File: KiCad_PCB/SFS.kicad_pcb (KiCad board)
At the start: 2 copper layers, 76.2 x 106.7 mm, 40 parts, among them J1 Screw_Terminal_01x08, J2 Conn_01x06, J4 Screw_Terminal_01x02, J6 Screw_Terminal_01x04, Q1 IRF9540N, Q2 IRLB4132, Q3 2N7000, SW1 SW_Push, SW2 SW_Push, U2 ADS1115, U3 ADS1115, U4 DS3231, U6 L7806, U7 LT1460

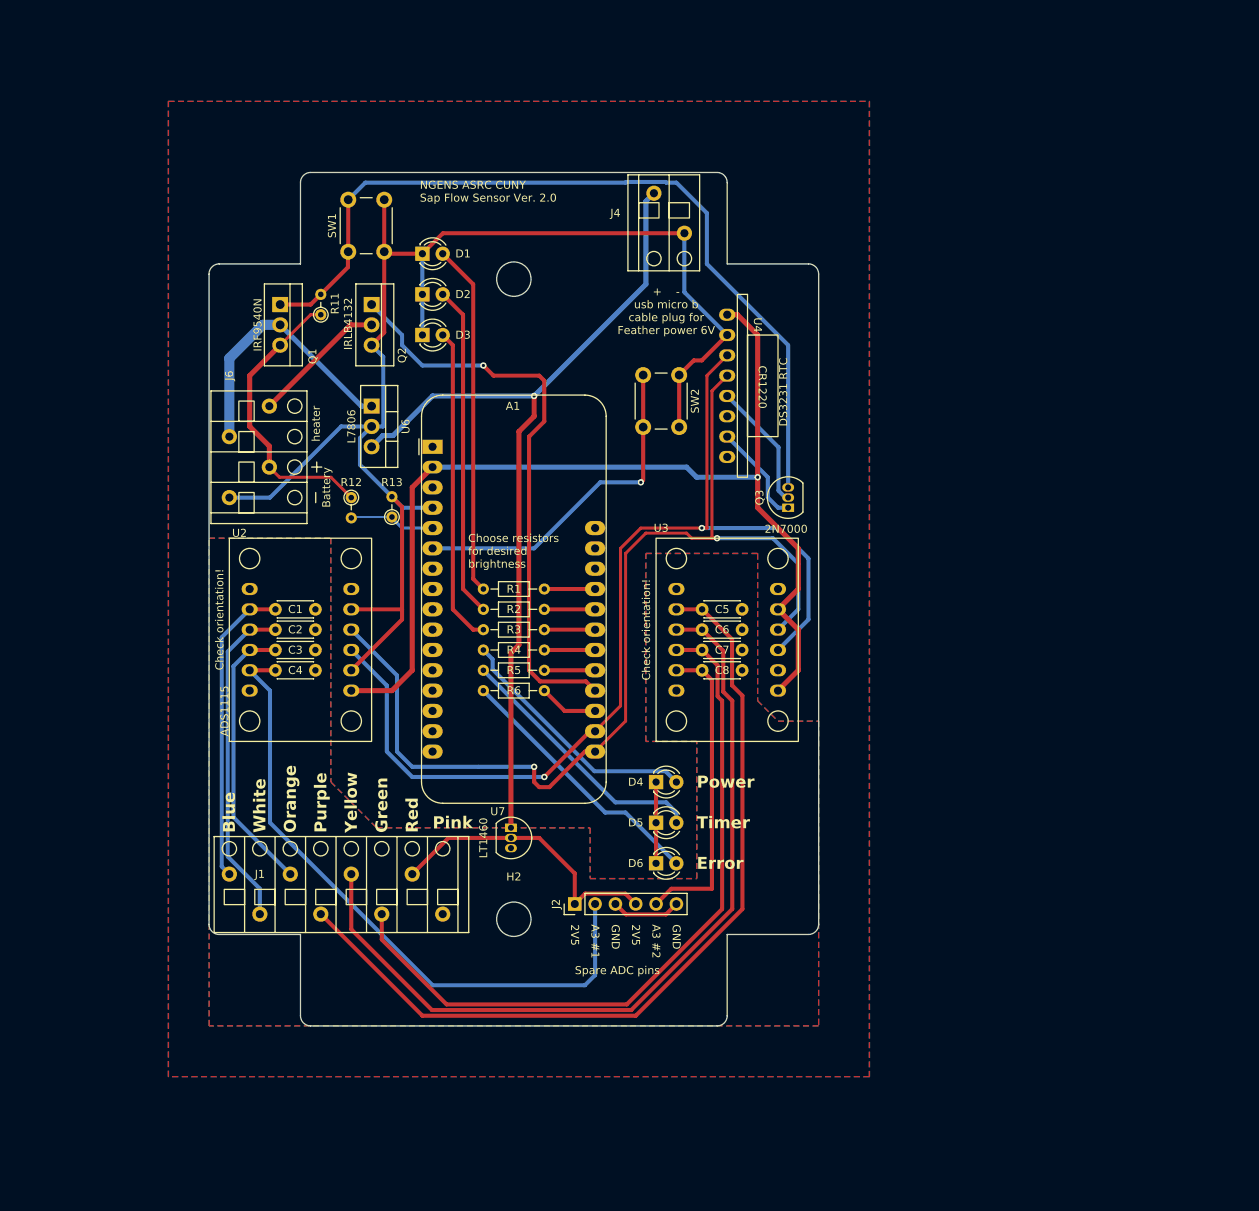
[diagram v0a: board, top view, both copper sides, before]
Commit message: updated kicad
Updated to v2.1 from evonne's github
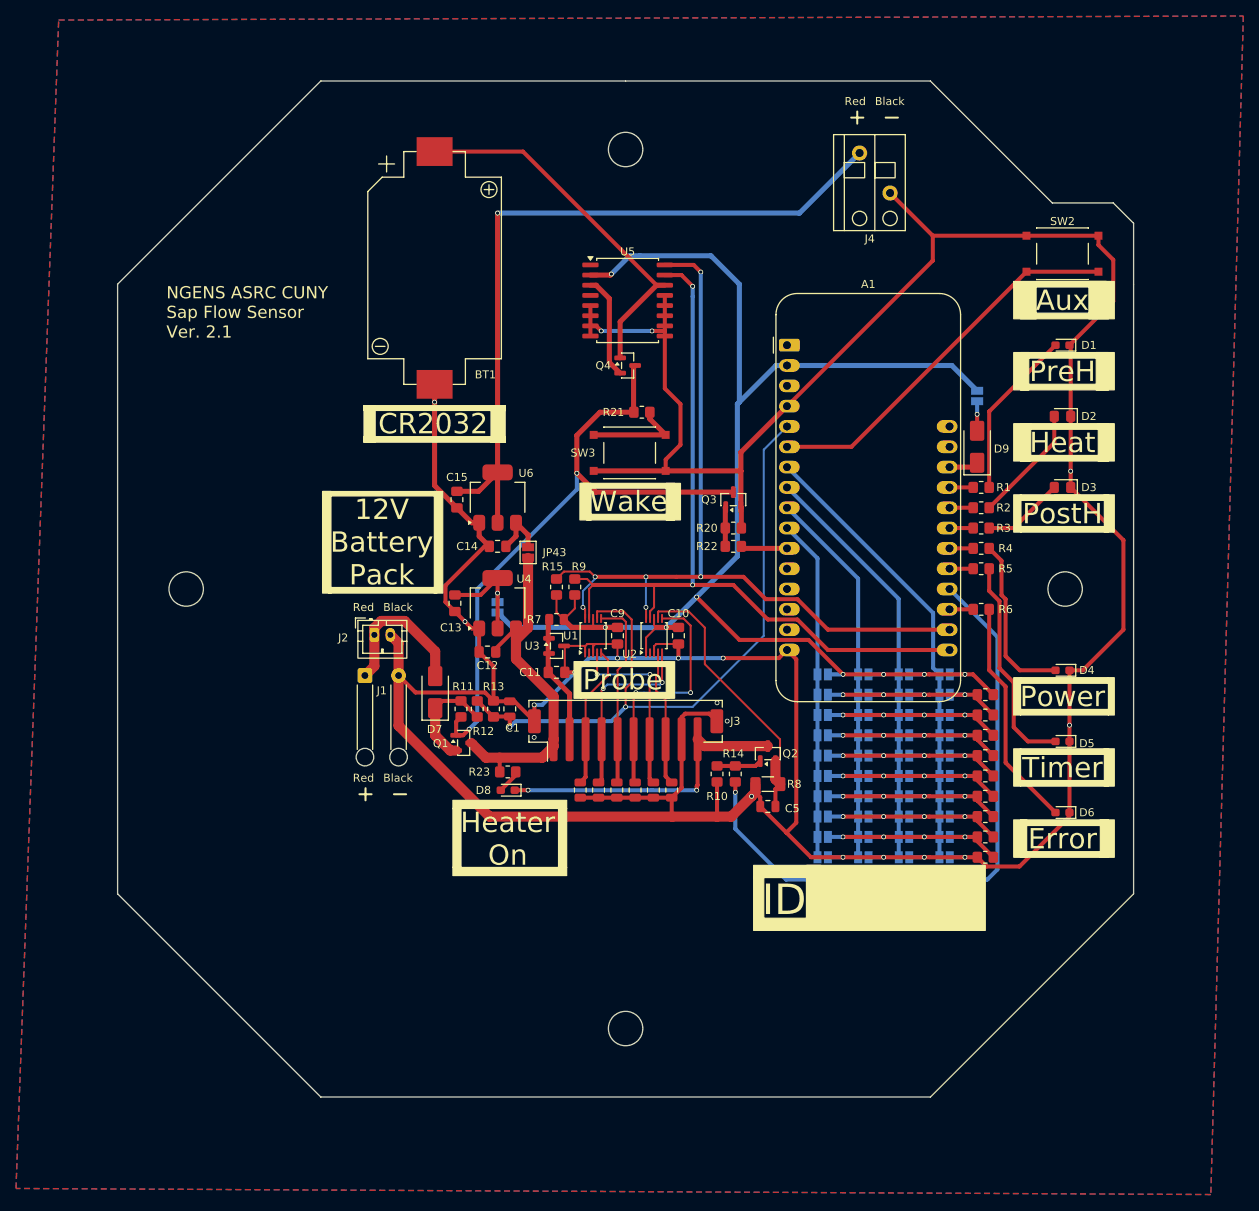
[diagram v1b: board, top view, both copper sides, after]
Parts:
- removed J6: Screw_Terminal_01x04, SapFlow_Footprints:Wurth_Screwless45_3.81mm_4
- removed SW1: SW_Push, Button_Switch_THT:SW_PUSH_6mm_H4.3mm
- removed U7: LT1460, Package_TO_SOT_THT:TO-92_Inline
- added BT1: CR2032, SapFlow_Footprints:BatteryHolder_MYOUNG_C964760_1x2032, F.Cu at (77.7, 61.5)
- added C10: 100n, Capacitor_SMD:C_0805_2012Metric_Pad1.18x1.45mm_HandSolder, F.Cu at (108.2, 107.4)
- added C11: 1u, Capacitor_SMD:C_0805_2012Metric_Pad1.18x1.45mm_HandSolder, F.Cu at (93.0, 112.0)
- added C12: 1u, Capacitor_SMD:C_0805_2012Metric_Pad1.18x1.45mm_HandSolder, F.Cu at (84.3, 109.5)
- added C13: 1u, Capacitor_SMD:C_0805_2012Metric_Pad1.18x1.45mm_HandSolder, F.Cu at (80.3, 103.4)
- added C14: 1u, Capacitor_SMD:C_0805_2012Metric_Pad1.18x1.45mm_HandSolder, F.Cu at (85.6, 96.3)
- added C15: 1u, Capacitor_SMD:C_0805_2012Metric_Pad1.18x1.45mm_HandSolder, F.Cu at (80.5, 90.4)
- added C9: 100n, Capacitor_SMD:C_0805_2012Metric_Pad1.18x1.45mm_HandSolder, F.Cu at (100.6, 107.4)
- added D7: SS14, Diode_SMD:D_SMA, F.Cu at (77.8, 114.5)
- added D8: Red, LED_SMD:LED_0603_1608Metric_Pad1.05x0.95mm_HandSolder, F.Cu at (86.9, 126.7)
- added D9: SS14, Diode_SMD:D_SMA, F.Cu at (145.5, 83.8)
- added H3: MountingHole, MountingHole:MountingHole_4.3mm_M4, F.Cu at (156.5, 101.6)
- added H4: MountingHole, MountingHole:MountingHole_4.3mm_M4, F.Cu at (101.6, 156.5)
- added J3: JST-PH, Connector_JST:JST_PH_B10B-PH-SM4-TB_1x10-1MP_P2.00mm_Vertical, F.Cu at (101.6, 119.9)
- added JP1: SolderJumper_2_Open, Jumper:SolderJumper-2_P1.3mm_Open_Pad1.0x1.5mm, B.Cu at (141.5, 112.3)
- added JP10: SolderJumper_2_Open, Jumper:SolderJumper-2_P1.3mm_Open_Pad1.0x1.5mm, B.Cu at (141.5, 135.1)
- added JP11: SolderJumper_2_Open, Jumper:SolderJumper-2_P1.3mm_Open_Pad1.0x1.5mm, B.Cu at (136.4, 112.3)
- added JP12: SolderJumper_2_Open, Jumper:SolderJumper-2_P1.3mm_Open_Pad1.0x1.5mm, B.Cu at (136.4, 114.8)
- added JP13: SolderJumper_2_Open, Jumper:SolderJumper-2_P1.3mm_Open_Pad1.0x1.5mm, B.Cu at (136.4, 117.3)
- added JP14: SolderJumper_2_Open, Jumper:SolderJumper-2_P1.3mm_Open_Pad1.0x1.5mm, B.Cu at (136.4, 119.9)
- added JP15: SolderJumper_2_Open, Jumper:SolderJumper-2_P1.3mm_Open_Pad1.0x1.5mm, B.Cu at (136.4, 122.4)
- added JP16: SolderJumper_2_Open, Jumper:SolderJumper-2_P1.3mm_Open_Pad1.0x1.5mm, B.Cu at (136.4, 125.0)
- added JP17: SolderJumper_2_Open, Jumper:SolderJumper-2_P1.3mm_Open_Pad1.0x1.5mm, B.Cu at (136.4, 127.5)
- added JP18: SolderJumper_2_Open, Jumper:SolderJumper-2_P1.3mm_Open_Pad1.0x1.5mm, B.Cu at (136.4, 130.0)
- added JP19: SolderJumper_2_Open, Jumper:SolderJumper-2_P1.3mm_Open_Pad1.0x1.5mm, B.Cu at (136.4, 132.6)
- added JP2: SolderJumper_2_Open, Jumper:SolderJumper-2_P1.3mm_Open_Pad1.0x1.5mm, B.Cu at (141.5, 114.8)
- added JP20: SolderJumper_2_Open, Jumper:SolderJumper-2_P1.3mm_Open_Pad1.0x1.5mm, B.Cu at (136.4, 135.1)
- added JP21: SolderJumper_2_Open, Jumper:SolderJumper-2_P1.3mm_Open_Pad1.0x1.5mm, B.Cu at (131.3, 112.3)
- added JP22: SolderJumper_2_Open, Jumper:SolderJumper-2_P1.3mm_Open_Pad1.0x1.5mm, B.Cu at (131.3, 114.8)
- added JP23: SolderJumper_2_Open, Jumper:SolderJumper-2_P1.3mm_Open_Pad1.0x1.5mm, B.Cu at (131.3, 117.3)
- added JP24: SolderJumper_2_Open, Jumper:SolderJumper-2_P1.3mm_Open_Pad1.0x1.5mm, B.Cu at (131.3, 119.9)
- added JP25: SolderJumper_2_Open, Jumper:SolderJumper-2_P1.3mm_Open_Pad1.0x1.5mm, B.Cu at (131.3, 122.4)
- added JP26: SolderJumper_2_Open, Jumper:SolderJumper-2_P1.3mm_Open_Pad1.0x1.5mm, B.Cu at (131.3, 125.0)
- added JP27: SolderJumper_2_Open, Jumper:SolderJumper-2_P1.3mm_Open_Pad1.0x1.5mm, B.Cu at (131.3, 127.5)
- added JP28: SolderJumper_2_Open, Jumper:SolderJumper-2_P1.3mm_Open_Pad1.0x1.5mm, B.Cu at (131.3, 130.0)
- added JP29: SolderJumper_2_Open, Jumper:SolderJumper-2_P1.3mm_Open_Pad1.0x1.5mm, B.Cu at (131.3, 132.6)
- added JP3: SolderJumper_2_Open, Jumper:SolderJumper-2_P1.3mm_Open_Pad1.0x1.5mm, B.Cu at (141.5, 117.3)
- added JP30: SolderJumper_2_Open, Jumper:SolderJumper-2_P1.3mm_Open_Pad1.0x1.5mm, B.Cu at (131.3, 135.1)
- added JP31: SolderJumper_2_Open, Jumper:SolderJumper-2_P1.3mm_Open_Pad1.0x1.5mm, B.Cu at (126.2, 112.3)
- added JP32: SolderJumper_2_Open, Jumper:SolderJumper-2_P1.3mm_Open_Pad1.0x1.5mm, B.Cu at (126.2, 114.8)
- added JP33: SolderJumper_2_Open, Jumper:SolderJumper-2_P1.3mm_Open_Pad1.0x1.5mm, B.Cu at (126.2, 117.3)
- added JP34: SolderJumper_2_Open, Jumper:SolderJumper-2_P1.3mm_Open_Pad1.0x1.5mm, B.Cu at (126.2, 119.9)
- added JP35: SolderJumper_2_Open, Jumper:SolderJumper-2_P1.3mm_Open_Pad1.0x1.5mm, B.Cu at (126.2, 122.4)
- added JP36: SolderJumper_2_Open, Jumper:SolderJumper-2_P1.3mm_Open_Pad1.0x1.5mm, B.Cu at (126.2, 125.0)
- added JP37: SolderJumper_2_Open, Jumper:SolderJumper-2_P1.3mm_Open_Pad1.0x1.5mm, B.Cu at (126.2, 127.5)
- added JP38: SolderJumper_2_Open, Jumper:SolderJumper-2_P1.3mm_Open_Pad1.0x1.5mm, B.Cu at (126.2, 130.0)
- added JP39: SolderJumper_2_Open, Jumper:SolderJumper-2_P1.3mm_Open_Pad1.0x1.5mm, B.Cu at (126.2, 132.6)
- added JP4: SolderJumper_2_Open, Jumper:SolderJumper-2_P1.3mm_Open_Pad1.0x1.5mm, B.Cu at (141.5, 119.9)
- added JP40: SolderJumper_2_Open, Jumper:SolderJumper-2_P1.3mm_Open_Pad1.0x1.5mm, B.Cu at (126.2, 135.1)
- added JP41: SolderJumper_2_Open, Jumper:SolderJumper-2_P1.3mm_Open_Pad1.0x1.5mm, B.Cu at (85.6, 103.9)
- added JP42: SolderJumper_2_Open, Jumper:SolderJumper-2_P1.3mm_Open_Pad1.0x1.5mm, B.Cu at (145.5, 77.5)
- added JP43: SolderJumper_2_Open, Jumper:SolderJumper-2_P1.3mm_Open_Pad1.0x1.5mm, F.Cu at (89.4, 97.0)
- added JP5: SolderJumper_2_Open, Jumper:SolderJumper-2_P1.3mm_Open_Pad1.0x1.5mm, B.Cu at (141.5, 122.4)
- added JP6: SolderJumper_2_Open, Jumper:SolderJumper-2_P1.3mm_Open_Pad1.0x1.5mm, B.Cu at (141.5, 125.0)
- added JP7: SolderJumper_2_Open, Jumper:SolderJumper-2_P1.3mm_Open_Pad1.0x1.5mm, B.Cu at (141.5, 127.5)
- added JP8: SolderJumper_2_Open, Jumper:SolderJumper-2_P1.3mm_Open_Pad1.0x1.5mm, B.Cu at (141.5, 130.0)
- added JP9: SolderJumper_2_Open, Jumper:SolderJumper-2_P1.3mm_Open_Pad1.0x1.5mm, B.Cu at (141.5, 132.6)
- added N1: Housing, SapFlow_Footprints:Enclosure_WH-10, F.Cu at (101.6, 101.6)
- added Q4: AO3400A, Package_TO_SOT_SMD:SOT-23, F.Cu at (101.9, 73.7)
- added R10: 100k, Resistor_SMD:R_0805_2012Metric_Pad1.20x1.40mm_HandSolder, F.Cu at (113.0, 124.7)
- added R14: 100R, Resistor_SMD:R_0805_2012Metric_Pad1.20x1.40mm_HandSolder, F.Cu at (115.3, 124.7)
- added R15: 10k, Resistor_SMD:R_0805_2012Metric_Pad1.20x1.40mm_HandSolder, F.Cu at (93.0, 101.3)
- added R20: 100k, Resistor_SMD:R_0805_2012Metric_Pad1.20x1.40mm_HandSolder, F.Cu at (115.1, 94.0)
- added R21: 1k, Resistor_SMD:R_0805_2012Metric_Pad1.20x1.40mm_HandSolder, F.Cu at (103.6, 79.5)
- added R22: 100R, Resistor_SMD:R_0805_2012Metric_Pad1.20x1.40mm_HandSolder, F.Cu at (115.1, 96.3)
- added R23: 22k, Resistor_SMD:R_0805_2012Metric_Pad1.20x1.40mm_HandSolder, F.Cu at (86.9, 124.5)
- added R24: 10k, Resistor_SMD:R_0805_2012Metric_Pad1.20x1.40mm_HandSolder, F.Cu at (146.6, 114.8)
- added R25: 10k, Resistor_SMD:R_0805_2012Metric_Pad1.20x1.40mm_HandSolder, F.Cu at (146.6, 117.3)
- added R26: 10k, Resistor_SMD:R_0805_2012Metric_Pad1.20x1.40mm_HandSolder, F.Cu at (146.6, 119.9)
- added R27: 10k, Resistor_SMD:R_0805_2012Metric_Pad1.20x1.40mm_HandSolder, F.Cu at (146.6, 122.4)
- added R28: 10k, Resistor_SMD:R_0805_2012Metric_Pad1.20x1.40mm_HandSolder, F.Cu at (146.6, 125.0)
- added R29: 10k, Resistor_SMD:R_0805_2012Metric_Pad1.20x1.40mm_HandSolder, F.Cu at (146.6, 127.5)
- added R30: 10k, Resistor_SMD:R_0805_2012Metric_Pad1.20x1.40mm_HandSolder, F.Cu at (146.6, 130.0)
- added R31: 10k, Resistor_SMD:R_0805_2012Metric_Pad1.20x1.40mm_HandSolder, F.Cu at (146.6, 132.6)
- added R32: 10k, Resistor_SMD:R_0805_2012Metric_Pad1.20x1.40mm_HandSolder, F.Cu at (146.6, 135.1)
- added R7: 390R, Resistor_SMD:R_0805_2012Metric, F.Cu at (93.0, 105.4)
- added R8: 1R, Resistor_SMD:R_1206_3216Metric_Pad1.30x1.75mm_HandSolder, F.Cu at (119.4, 126.0)
- added R9: 10k, Resistor_SMD:R_0805_2012Metric_Pad1.20x1.40mm_HandSolder, F.Cu at (95.2, 101.3)
- added SW3: SW_Push, AAA_Library:SW_Push_1P1T_NO_6x6mm_H9.5mm_C2837532, F.Cu at (102.1, 84.6)
- added U1: ADS1115IDGS, Package_SO:TSSOP-10_3x3mm_P0.5mm, F.Cu at (97.5, 107.4)
- added U5: DS3231M, Package_SO:SOIC-16W_7.5x10.3mm_P1.27mm, F.Cu at (101.9, 65.5)
- C1, C2, C3, C4, C5, C6, C7, C8: footprint Capacitor_THT:C_Disc_D4.3mm_W1.9mm_P5.00mm -> Capacitor_SMD:C_0805_2012Metric
- D1, D4, D5, D6: value LED -> Red; footprint LED_THT:LED_D3.0mm -> LED_SMD:LED_0603_1608Metric_Pad1.05x0.95mm_HandSolder
- D2: value LED -> Yellow; footprint LED_THT:LED_D3.0mm -> LED_SMD:LED_0805_2012Metric_Pad1.15x1.40mm_HandSolder
- D3: value LED -> Green; footprint LED_THT:LED_D3.0mm -> LED_SMD:LED_0805_2012Metric_Pad1.15x1.40mm_HandSolder
- J1: value Screw_Terminal_01x08 -> Wires; footprint SapFlow_Footprints:Wurth_Screwless45_3.81mm_8 -> Connector_Wire:SolderWire-0.25sqmm_1x02_P4.2mm_D0.65mm_OD1.7mm_Relief
- J2: value Conn_01x06 -> JST-PH; footprint Connector_PinHeader_2.54mm:PinHeader_1x06_P2.54mm_Vertical -> Connector_JST:JST_PH_B2B-PH-K_1x02_P2.00mm_Vertical
- Q1: value IRF9540N -> AO3401A; footprint Package_TO_SOT_THT:TO-262-3_Vertical -> Package_TO_SOT_SMD:SOT-23
- Q2: value IRLB4132 -> AO3400A; footprint Package_TO_SOT_THT:TO-262-3_Vertical -> Package_TO_SOT_SMD:SOT-23
- Q3: value 2N7000 -> AO3400A; footprint Package_TO_SOT_THT:TO-92_Inline -> Package_TO_SOT_SMD:SOT-23
- R1, R4, R5, R6: value 10k -> 3k3; footprint Resistor_THT:R_Axial_DIN0204_L3.6mm_D1.6mm_P7.62mm_Horizontal -> Resistor_SMD:R_0805_2012Metric_Pad1.20x1.40mm_HandSolder
- R11: value 100K -> 100k; footprint Resistor_THT:R_Axial_DIN0204_L3.6mm_D1.6mm_P2.54mm_Vertical -> Resistor_SMD:R_0805_2012Metric_Pad1.20x1.40mm_HandSolder
- R12, R13: footprint Resistor_THT:R_Axial_DIN0204_L3.6mm_D1.6mm_P2.54mm_Vertical -> Resistor_SMD:R_0805_2012Metric_Pad1.20x1.40mm_HandSolder
- R2: value 10k -> 1k5; footprint Resistor_THT:R_Axial_DIN0204_L3.6mm_D1.6mm_P7.62mm_Horizontal -> Resistor_SMD:R_0805_2012Metric_Pad1.20x1.40mm_HandSolder
- R3: value 10k -> 6k8; footprint Resistor_THT:R_Axial_DIN0204_L3.6mm_D1.6mm_P7.62mm_Horizontal -> Resistor_SMD:R_0805_2012Metric_Pad1.20x1.40mm_HandSolder
- SW2: footprint Button_Switch_THT:SW_PUSH_6mm_H4.3mm -> AAA_Library:SW_Push_1P1T_NO_6x6mm_H9.5mm_C2837532
- U2: value ADS1115 -> ADS1115IDGS; footprint SapFlow_Footprints:ADS1115_Breakout -> Package_SO:TSSOP-10_3x3mm_P0.5mm
- U3: value ADS1115 -> TL431DBZ; footprint SapFlow_Footprints:ADS1115_Breakout -> Package_TO_SOT_SMD:SOT-23
- U4: value DS3231 -> AMS1117-3.3; footprint SapFlow_Footprints:DS3231_Breakout_RightAngle -> Package_TO_SOT_SMD:SOT-223-3_TabPin2
- U6: value L7806 -> AMS1117-5.0; footprint Package_TO_SOT_THT:TO-220-3_Vertical -> Package_TO_SOT_SMD:SOT-223-3_TabPin2
- moved D3 82.2 mm to (156.2, 88.9), turned to 180 degrees
- moved D2 81.4 mm to (156.2, 80.0), turned to 180 degrees
- moved D1 80.8 mm to (156.2, 71.1), turned to 180 degrees
- moved Q2 74.9 mm to (119.4, 122.2), turned to 90 degrees
- moved Q1 59.4 mm to (81.4, 120.8), turned to 0 degrees
- moved H2 58.1 mm to (46.7, 101.6)
- moved R1 56.1 mm to (146.1, 88.9), turned to 0 degrees
- moved R2 56.1 mm to (146.1, 91.4), turned to 0 degrees
- moved R3 56.1 mm to (146.1, 94.0), turned to 0 degrees
- moved R4 56.1 mm to (146.1, 96.5), turned to 0 degrees
- moved R5 56.1 mm to (146.1, 99.1), turned to 0 degrees
- moved R6 55.5 mm to (146.1, 104.1), turned to 0 degrees
- moved D4 52.7 mm to (156.2, 111.8), turned to 180 degrees
- moved R11 52.3 mm to (81.0, 116.6), turned to -90 degrees
- moved D5 51.8 mm to (156.2, 120.7), turned to 180 degrees
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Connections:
- net Net-(Q1-G) renamed /RTC/~{POWER_ON}
- A1 pad 10: unconnected-(A1-A5-Pad10) -> /ID/ID_0
- A1 pad 11: unconnected-(A1-SCK/D24-Pad11) -> /RTC/KEEP_ON
- A1 pad 26: unconnected-(A1-USB-Pad26) -> Net-(A1-USB)
- A1 pad 5: Net-(A1-DAC0/A0) -> /Vbat_sense
- A1 pad 7: unconnected-(A1-A2-Pad7) -> /ID/ID_3
- A1 pad 8: unconnected-(A1-A3-Pad8) -> /ID/ID_2
- A1 pad 9: unconnected-(A1-A4-Pad9) -> /ID/ID_1
- C1 pad 1: Net-(J1-Pin_1) -> /Vbat_sense
- C1 pad 2: GNDA -> GND
- C2 pad 1: Net-(J1-Pin_2) -> Net-(J3-Pin_5)
- C2 pad 2: GNDA -> GND
- C3 pad 1: Net-(J1-Pin_3) -> Net-(J3-Pin_3)
- C3 pad 2: GNDA -> GND
- C4 pad 1: Net-(J2-Pin_2) -> Net-(J3-Pin_7)
- C4 pad 2: GNDA -> GND
- C5 pad 1: Net-(J1-Pin_4) -> /Probe/CURRENT_SENSE
- C5 pad 2: GNDA -> GND
- C6 pad 1: Net-(J1-Pin_5) -> Net-(J3-Pin_6)
- C6 pad 2: GNDA -> GND
- C7 pad 1: Net-(J1-Pin_6) -> Net-(J3-Pin_4)
- C7 pad 2: GNDA -> GND
- C8 pad 1: Net-(J2-Pin_5) -> Net-(J3-Pin_8)
- C8 pad 2: GNDA -> GND
- J1 pad 1: Net-(J1-Pin_1) -> Net-(D7-A)
- J1 pad 2: Net-(J1-Pin_2) -> GND
- J2 pad 1: /Analog/2V5 -> Net-(D7-A)
- J2 pad 2: Net-(J2-Pin_2) -> GND
- J4 pad 2: +6V -> Net-(J4-Pin_2)
- Q1 pad 2: Net-(J6-Pin_2) -> /Vbat
- Q1 pad 3: Net-(J6-Pin_3) -> /Probe/HEAT+
- Q2 pad 1: HEAT -> Net-(Q2-G)
- Q2 pad 2: Net-(J6-Pin_1) -> /Probe/CURRENT_SENSE
- Q2 pad 3: GND -> Net-(D8-K)
- Q3 pad 1: Net-(Q3-S) -> Net-(Q3-G)
- Q3 pad 2: Net-(Q3-G) -> GND
- R11 pad 1: Net-(J6-Pin_3) -> /Vbat
- R12 pad 1: Net-(J6-Pin_3) -> /Vbat
- R12 pad 2: Net-(A1-DAC0/A0) -> /Vbat_sense
- R13 pad 1: Net-(A1-DAC0/A0) -> /Vbat_sense
- U2 pad 10: Net-(J1-Pin_3) -> SCL
- U2 pad 2: GND -> unconnected-(U2-ALERT/RDY-Pad2)
- U2 pad 3: SCL -> GND
- U2 pad 4: SDA -> Net-(J3-Pin_8)
- U2 pad 5: GND -> Net-(J3-Pin_4)
- U2 pad 6: unconnected-(U2-ALRT-Pad6) -> Net-(J3-Pin_6)
- U2 pad 7: GNDA -> /Probe/CURRENT_SENSE
- U2 pad 8: Net-(J1-Pin_1) -> +3V3
- U2 pad 9: Net-(J1-Pin_2) -> SDA
- U3 pad 1: +3V3 -> +2V5
- U3 pad 2: GND -> +2V5
- U3 pad 3: SCL -> GND
- U4 pad 1: +3V3 -> GND
- U4 pad 2: GND -> Net-(JP41-B)
- U4 pad 3: SCL -> /Probe/HEAT+
- U6 pad 1: Net-(J6-Pin_2) -> GND
- U6 pad 2: GND -> Net-(J4-Pin_2)
- U6 pad 3: +6V -> Net-(JP43-B)
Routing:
- net GND: track 188.9 -> 512.0 mm, vias 0 -> 19
- net +6V: track 109.7 -> 0.00 mm, vias 1 -> 0
- net Net-(J1-Pin_4): track 106.3 -> 0.00 mm
- net Net-(J1-Pin_5): track 103.6 -> 0.00 mm
- net Net-(J4-Pin_2): track 0.00 -> 93.1 mm, vias 0 -> 1
- net Net-(J1-Pin_6): track 90.9 -> 0.00 mm
- net /Vbat_sense: track 0.00 -> 86.9 mm, vias 0 -> 2
- net Net-(J2-Pin_2): track 81.8 -> 0.00 mm
- net +3V3: track 130.9 -> 195.7 mm, vias 1 -> 8
- net /ID/ID_3: track 0.00 -> 56.7 mm
- net /ID/ID_2: track 0.00 -> 52.0 mm
- net /ID/ID_1: track 0.00 -> 47.4 mm
- net Net-(BT1-+): track 0.00 -> 46.7 mm
- net /Probe/HEAT+: track 0.00 -> 46.4 mm
- net /ID/ID_0: track 0.00 -> 42.7 mm
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- removed copper zone on B.Cu, net GNDA
- removed copper zone on F.Cu, net GNDA
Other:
- board size 76.2 x 106.7 mm -> 127 x 127 mm
- board text added: "12V Battery Pack"
- board text added: "9 8 7 6 5 4 3 2 1 0"
- board text added: "Aux"
- board text added: "Black"
- board text added: "CONNECTOR"
- board text added: "CR2032"
- board text added: "Heat"
- board text added: "Heater On"
- board text added: "ID"
- board text added: "NGENS ASRC CUNY Sap Flow Sensor Ver. 2.1"
- board text added: "PostH"
- board text added: "PreH"
- board text added: "Probe"
- board text added: "SD card with tape"
- board text added: "USB pig tail"
- board text added: "Wake"
- board text removed: "+ - usb micro b cable plug for Feather power 6V"
- board text removed: "2V5"
- board text removed: "A3 #1"
- board text removed: "A3 #2"
- board text removed: "ADS1115"
- board text removed: "Battery"
- board text removed: "Blue"
- board text removed: "Check orientation!"
- board text removed: "Choose resistors for desired brightness"
- board text removed: "DS3231 RTC"
- board text removed: "Enclosure"
- board text removed: "GND"
- board text removed: "Green"
- board text removed: "NGENS ASRC CUNY Sap Flow Sensor Ver. 2.0"
- board text removed: "Orange"
- board text removed: "Pink"
- board text removed: "Purple"
- board text removed: "Spare ADC pins"
- board text removed: "White"
- board text removed: "Yellow"
- board text removed: "heater"
